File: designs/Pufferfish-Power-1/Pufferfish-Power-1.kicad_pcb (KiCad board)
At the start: 2 copper layers, 196 parts, among them J1 POWER_JACK_PTH, J2 POWER_JACK_PTH, J3 Molex_PicoFlex_20_Vertical, J4 Molex_MicroFit3_2x4_Receptacle, J5 Molex_MicroFit_2P, J6 Molex_MicroFit_2P, Q1 SiR158DP, Q10 2N7002E, Q11 2N7002E, Q12 2N7002E, Q13 2N7002E, Q14 2N7002E, Q14 TP0610T, Q15 2N7002E, Q15 TP0610T, Q16 2N7002E, Q16 TP0610T, Q17 2N7002E, Q17 TP0610T, Q18 2N7002E, Q18 TP0610T, Q19 2N7002E, Q19 TP0610T, Q2 SiR158DP, Q3 SiR158DP, Q4 SiR158DP, Q5 2N7002E, Q6 SiSS27DN, Q7 SiSS27DN, Q8 TP0610T, Q9 2N7002E, U1 LTC4421IUHE, U2 TPS568215RNN, U3 TPS82130

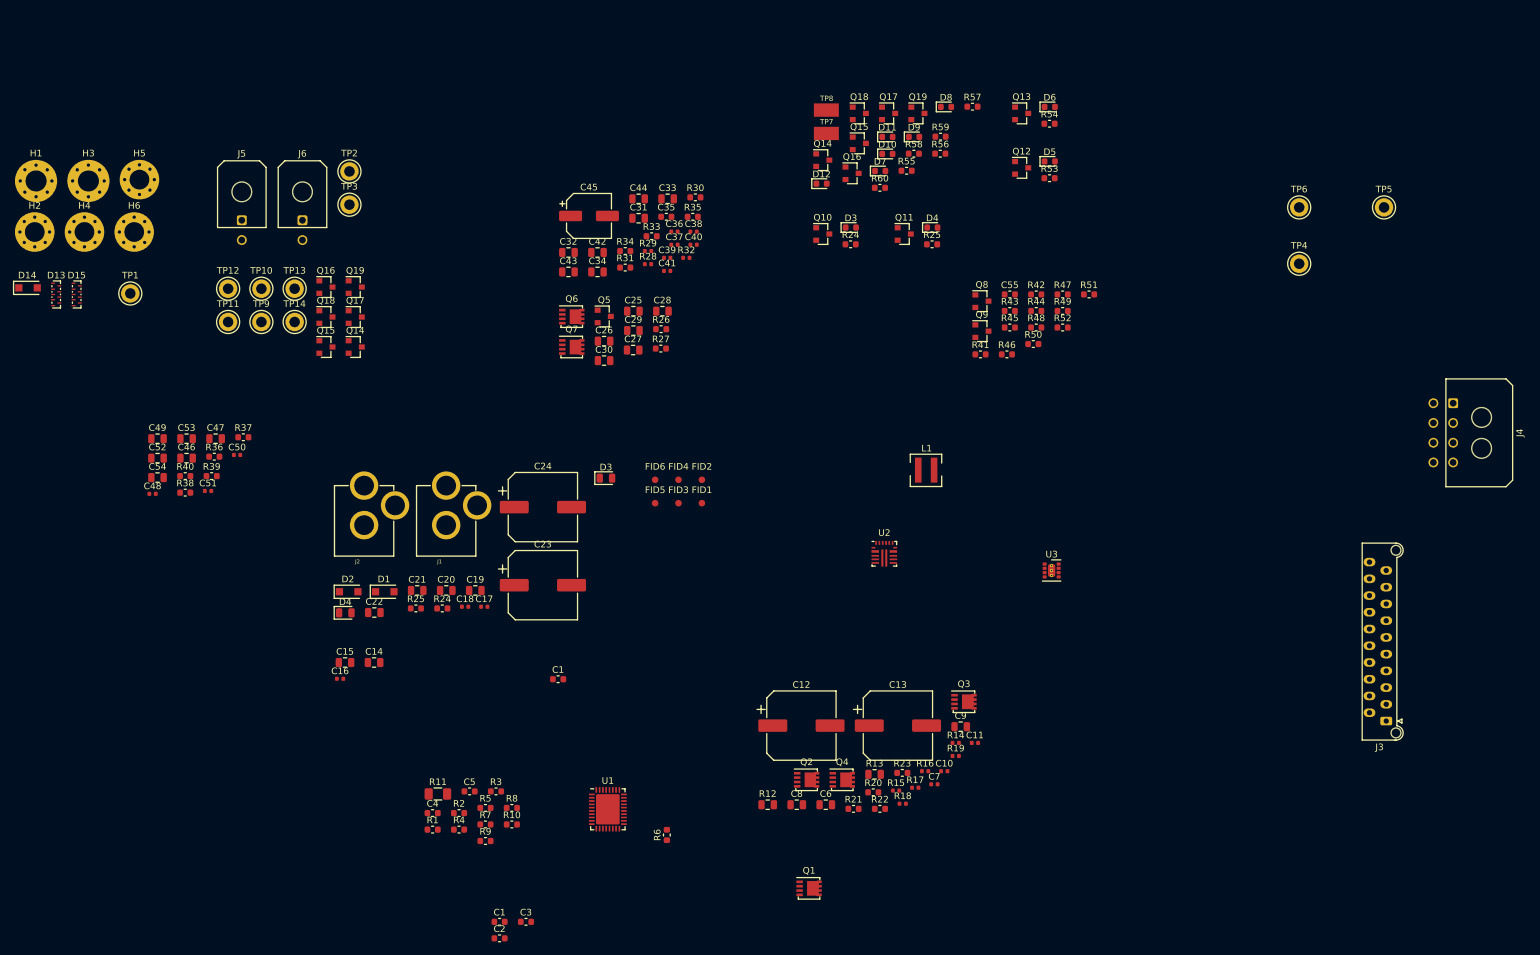
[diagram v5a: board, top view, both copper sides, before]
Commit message: Initial board layout, routing completed
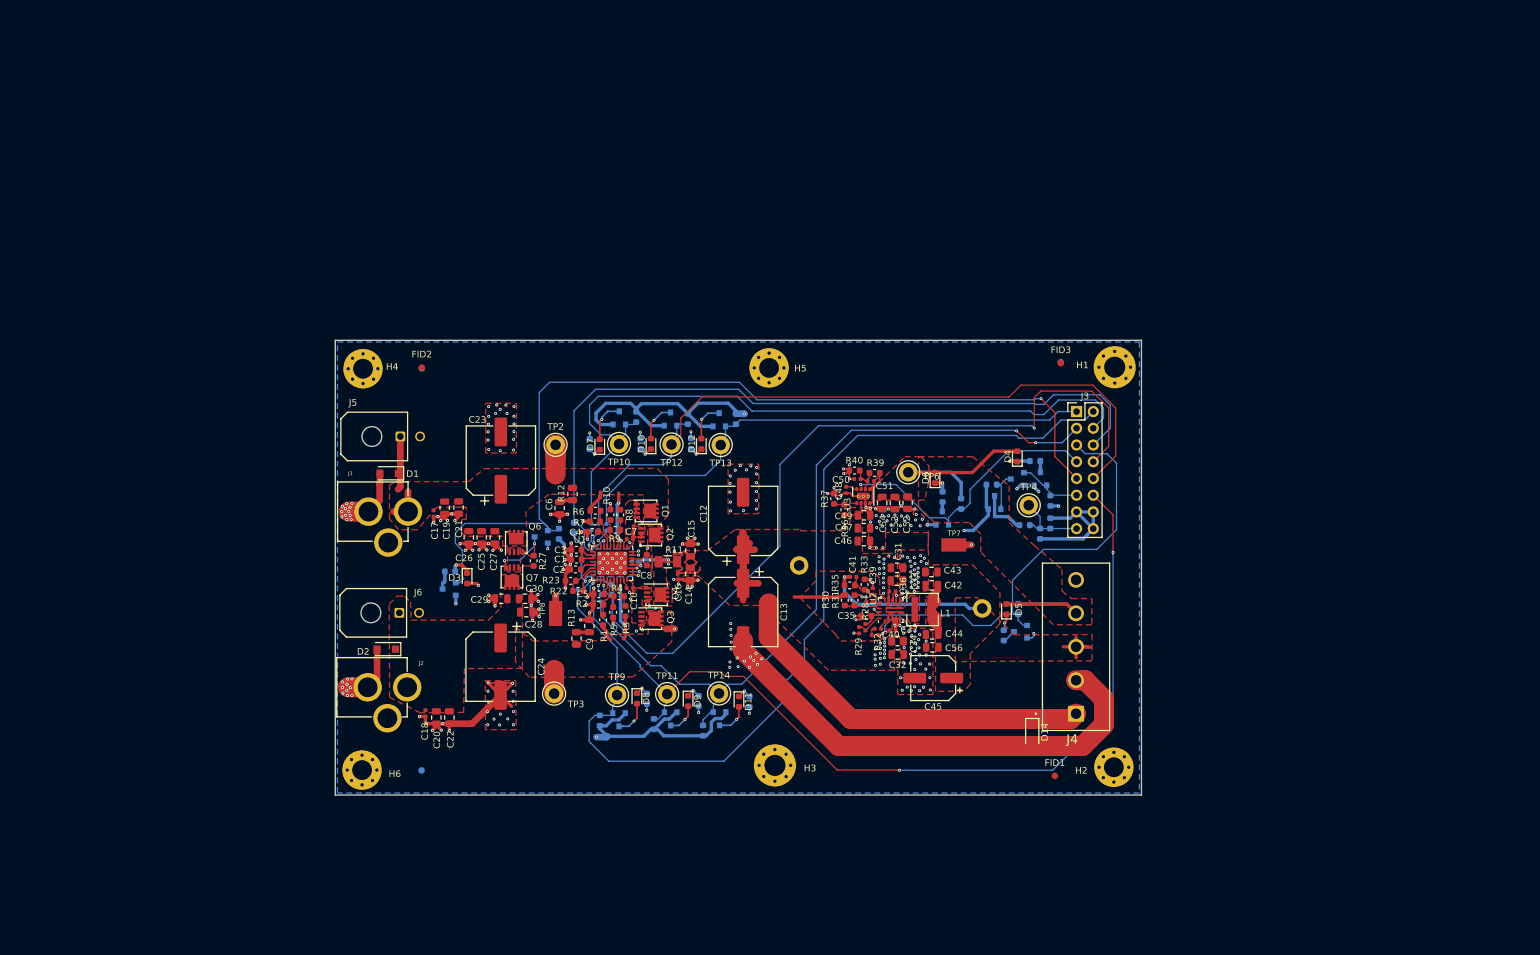
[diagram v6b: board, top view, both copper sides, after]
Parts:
- removed the C1 at (124.5, 119.4)
- removed D13, D15: ESDLC5V0PB8, Package_DFN_QFN:UDFN-9_1.0x3.8mm_P0.5mm
- removed the D3 at (168.9, 50.8)
- removed the D3 at (131.7, 88.8)
- removed the D4 at (92.2, 109.3)
- removed the Q14 at (164.6, 40.6)
- removed the Q15 at (170.2, 38.0)
- removed the Q16 at (169.1, 42.6)
- removed the Q17 at (174.6, 33.5)
- removed the Q18 at (170.2, 33.5)
- removed the Q19 at (179.1, 33.5)
- removed the R24 at (106.9, 108.6)
- removed the R25 at (102.9, 108.6)
- removed R45, R46: RES_10K_0603_SMD, Pufferfish:RES_SMD_0603
- added C56: CAP_22uF_25V_X5R_0805, Pufferfish:CAP_SMD_0805, F.Cu at (181.3, 114.5)
- added D3: LED_SMD_0603_YELLOW, LED_SMD:LED_0603_1608Metric, F.Cu at (110.6, 104.1)
- C11, C55, FID4, FID5, FID6, Q10, Q11, Q12, Q13, Q14, Q15, Q16, Q17, Q18, Q19, Q5, Q8, Q9, R14, R15, R16, R17, R18, R19, R20, R21, R24, R25, R26, R34, R38, R41, R42, R43, R44, R47, R48, R49, R50, R51, R52, R53, R54, R55, R56, R57, R58, R59, R60, TP1, TP5: moved to B.Cu
- C8: footprint Pufferfish:CAP_SMD_0805 -> Pufferfish:CAP_SMD_0603
- J3: value Molex_PicoFlex_20_Vertical -> 5103308-3; footprint Connector_Molex:Molex_Picoflex_90325-0020_2x10_P1.27mm_Vertical -> Connector_PinHeader_2.54mm:PinHeader_2x08_P2.54mm_Vertical
- J4: value Molex_MicroFit3_2x4_Receptacle -> Screw_Terminal_01x05; footprint Connector_Molex:Molex_Micro-Fit_3.0_43045-0800_2x04_P3.00mm_Horizontal -> Pufferfish:CUI_TB004-508-05BE
- moved H2 182.9 mm to (208.8, 132.7)
- moved D14 166.8 mm to (196.4, 127.5), turned to 270 degrees
- moved H1 166.2 mm to (209.0, 72.0)
- moved H3 136.9 mm to (157.4, 132.5)
- moved R38 117.8 mm to (185.6, 92.7), turned to 270 degrees
- moved C52 114.1 mm to (177.5, 92.6), turned to 270 degrees
- moved C54 110.1 mm to (173.7, 92.6), turned to 270 degrees
- moved TP1 109.6 mm to (161.1, 102.1)
- moved C53 108.0 mm to (175.6, 92.6), turned to 270 degrees
- moved C49 107.9 mm to (170.9, 94.5)
- moved C48 105.3 mm to (168.2, 90.7), turned to 270 degrees
- moved C46 103.6 mm to (170.9, 98.4)
- moved R40 101.6 mm to (169.5, 87.7), turned to 180 degrees
- moved D8 101.3 mm to (136.4, 122.3), turned to 270 degrees
- moved R39 100.7 mm to (172.5, 88.1), turned to 180 degrees
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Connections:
- net Net-(R22-Pad2) renamed /LTC4221/LTC4421-RETRY
- net Net-(R36-Pad2) renamed /3.3V Buck/3V3-EN
- C10 pad 1: /LTC4221/LTC4421-SOURCE2 -> /LTC4221/LTC4421-GATE2
- C10 pad 2: /LTC4221/LTC4421-GATE2 -> /LTC4221/LTC4421-SRC2
- C8 pad 2: VSYS-12V0 -> /LTC4221/LTC4421-CPO
- J3 pad 1: LTC4421-PWR-nDISABLE1 -> LTC4421-PWR-nCH1
- J3 pad 10: LTC4421-PWR-nCH2 -> LTC4421-PWR-nVALID1
- J3 pad 11: GND -> /Interface/BAT-MEAS-EN
- J3 pad 13: 3V3-PGOOD -> GND
- J3 pad 14: LTC4421-PWR-nFAULT2 -> GND
- J3 pad 15: GND -> /Interface/BAT-MEAS-ANALOG
- J3 pad 2: LTC4421-PWR-nCH1 -> LTC4421-PWR-nFAULT2
- J3 pad 3: GND -> LTC4421-PWR-nCH2
- J3 pad 4: LTC4421-PWR-nVALID1 -> LTC4421-PWR-nFAULT1
- J3 pad 5: LTC4421-PWR-nDISABLE2 -> VSYS-5V0-PGOOD
- J3 pad 6: LTC4421-PWR-nFAULT1 -> LTC4421-PWR-nDISABLE1
- J3 pad 7: GND -> 3V3-PGOOD
- J3 pad 8: BAT-CHARGE-EN -> LTC4421-PWR-nDISABLE2
- J3 pad 9: VSYS-5V0-PGOOD -> BAT-CHARGE-EN
- J4 pad 2: VSYS-12V0 -> GND
- J4 pad 3: GND -> VSYS-5V0
- J4 pad 4: GND -> VSYS-3V3
- J4 pad 5: VSYS-3V3 -> GND
- J6 pad 1: Net-(J6-Pad1) -> VIN-BACKUP-12V0
- Q3 pad 1: /LTC4221/LTC4421-GATE2 -> /LTC4221/LTC4421-SRC2
- Q3 pad 2: /LTC4221/LTC4421-GATE2 -> /LTC4221/LTC4421-SRC2
- Q3 pad 3: /LTC4221/LTC4421-GATE2 -> /LTC4221/LTC4421-SRC2
- Q3 pad 4: /LTC4221/LTC4421-SOURCE2 -> /LTC4221/LTC4421-GATE2
- Q4 pad 1: /LTC4221/LTC4421-GATE2 -> /LTC4221/LTC4421-SRC2
- Q4 pad 2: /LTC4221/LTC4421-GATE2 -> /LTC4221/LTC4421-SRC2
- Q4 pad 3: /LTC4221/LTC4421-GATE2 -> /LTC4221/LTC4421-SRC2
- Q4 pad 4: /LTC4221/LTC4421-SOURCE2 -> /LTC4221/LTC4421-GATE2
- TP3 pad 1: Net-(TP3-Pad1) -> VIN-BACKUP-12V0
- TP4 pad 1: Net-(Q8-Pad3) -> /Interface/BAT-MEAS-ANALOG
- TP5 pad 1: Net-(TP5-Pad1) -> VSYS-5V0
- U1 pad 27: /LTC4221/LTC4421-SOURCE2 -> /LTC4221/LTC4421-GATE2
- U1 pad 28: /LTC4221/LTC4421-GATE2 -> /LTC4221/LTC4421-SRC2
- U1 pad 33: VSYS-12V0 -> /LTC4221/LTC4421-CPO
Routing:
- net GND: track 0.00 -> 305.8 mm, vias 0 -> 293
- net VSYS-3V3: track 0.00 -> 254.7 mm, vias 0 -> 3
- net VSYS-12V0: track 0.00 -> 149.1 mm, vias 0 -> 35
- net LTC4421-PWR-nFAULT2: track 0.00 -> 145.8 mm
- net BAT-CHARGE-EN: track 0.00 -> 140.0 mm, vias 0 -> 1
- net LTC4421-PWR-nVALID2: track 0.00 -> 136.6 mm, vias 0 -> 2
- net LTC4421-PWR-nDISABLE2: track 0.00 -> 121.3 mm, vias 0 -> 2
- net LTC4421-PWR-nDISABLE1: track 0.00 -> 118.4 mm, vias 0 -> 1
- net LTC4421-PWR-nCH2: track 0.00 -> 116.4 mm, vias 0 -> 2
- net LTC4421-PWR-nFAULT1: track 0.00 -> 112.4 mm
- net LTC4421-PWR-nVALID1: track 0.00 -> 110.8 mm
- net LTC4421-PWR-nCH1: track 0.00 -> 83.4 mm
- net VIN-BACKUP-12V0: track 0.00 -> 78.3 mm, vias 0 -> 4
- net VSYS-5V0-PGOOD: track 0.00 -> 68.8 mm, vias 0 -> 1
- net VSYS-5V0: track 0.00 -> 46.9 mm, vias 0 -> 1
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- added copper zone on F.Cu, net /5V Buck/5V-BUCK-SW
- added copper zone on F.Cu, net /Input Connectors/CHARGER-DIODE
- added copper zone on F.Cu, net /LTC4221/LTC4421-SENSE
- added copper zone on F.Cu, net /LTC4221/LTC4421-SRC1
- added copper zone on F.Cu, net /LTC4221/LTC4421-SRC2
- added copper zone on B.Cu, net GND
- added copper zone on F.Cu, net GND
- added copper zone on In1.Cu, net GND
- added copper zone on In2.Cu, net GND
- added copper zone on F.Cu, net VIN-BACKUP-12V0
- added copper zone on F.Cu, net VIN-PRIMARY-12V0
- added copper zone on F.Cu, net VSYS-12V0
- added copper zone on In2.Cu, net VSYS-12V0
- added copper zone on F.Cu, net VSYS-3V3
- added copper zone on F.Cu, net VSYS-5V0
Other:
- board outline added: 122.4 x 69 mm
- copper layers 2 -> 4
- net class Default: clearance 0.2 -> 0.1524; trace_width 0.25 -> 0.1016; via_dia 0.8 -> 0.4572; via_drill 0.4 -> 0.2032
- rule pad_to_mask_clearance: 0.051 -> 0.0508
- rule solder_mask_min_width: 0.25 -> 0.254
- rule trace_clearance: 0.2 -> 0.1524
- rule trace_min: 0.2 -> 0.0762
- rule via_min_drill: 0.3 -> 0.1524
- rule via_min_size: 0.4 -> 0.3556

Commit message: - Added gerbers - Updated layout with silkscreen and DRC
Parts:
- added G***: LOGO, Pufferfish:LOGO_PUFFERFISH, F.Cu at (161.6, 84.2)
- TP1: moved to F.Cu
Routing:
- net GND: track 305.8 -> 301.4 mm, vias 293 -> 830
- net VIN-PRIMARY-12V0: track 33.2 -> 31.0 mm
- net VSYS-5V0: track 46.9 -> 45.5 mm
- net VSYS-12V0: track 149.1 -> 147.9 mm, vias 35 -> 34
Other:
- board text added: "1"
- board text added: "12V"
- board text added: "12V Backup"
- board text added: "12V Out"
- board text added: "12V Primary"
- board text added: "15"
- board text added: "16"
- board text added: "2"
- board text added: "3.3V"
- board text added: "3.3V PGOOD"
- board text added: "5V"
- board text added: "5V PGOOD"
- board text added: "Batt. Meas. Active"
- board text added: "Batt. Measurement"
- board text added: "Control Interface"
- board text added: "GND"
- board text added: "Power Module v1.0"
- board text added: "Power Output"
- board text added: "Primary Active"
- board text added: "Primary Fault"
- board text added: "Primary Valid"
- board text added: "Pufferfish"
- board text added: "S/N"
- board text added: "Secondary Active"
- board text added: "Secondary Fault"
- board text added: "Secondary Valid"

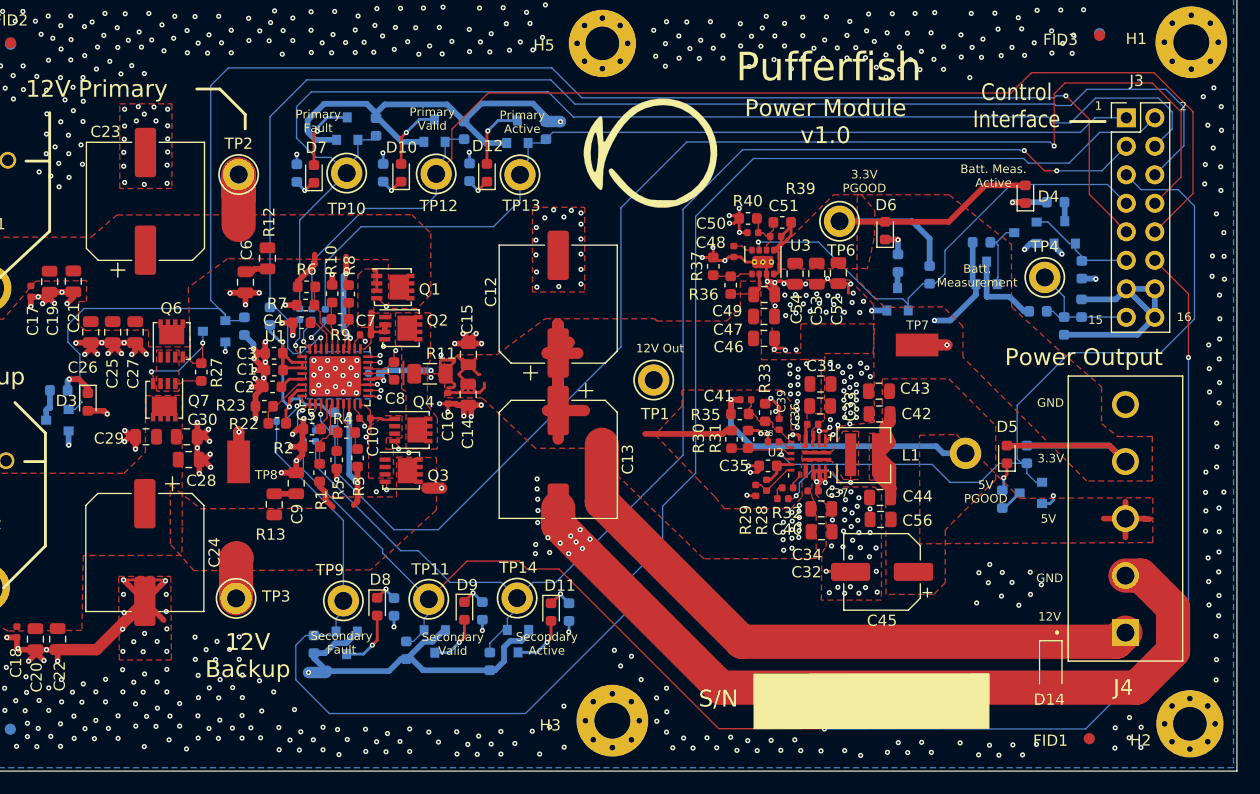
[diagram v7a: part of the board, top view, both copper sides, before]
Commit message: - Updated track width per DFM recommendations
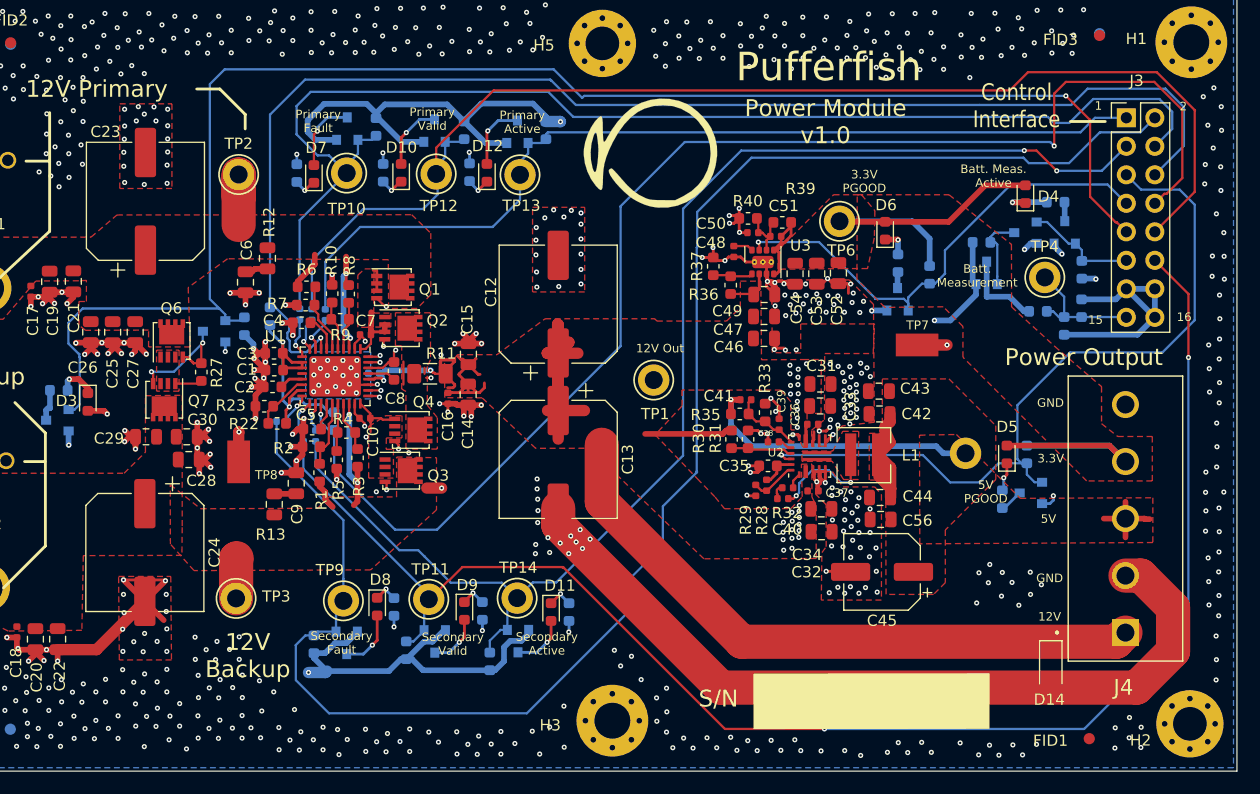
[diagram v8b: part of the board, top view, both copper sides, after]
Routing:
- net BAT-CHARGE-EN: track 140.0 -> 138.7 mm
- net /LTC4221/LTC4421-SENSE: track 18.2 -> 17.0 mm
- net VSYS-12V0: track 147.9 -> 146.9 mm
- net 3V3-PGOOD: track 43.0 -> 43.7 mm
- net VSYS-5V0-PGOOD: track 68.8 -> 69.5 mm
- net LTC4421-PWR-nDISABLE2: track 121.3 -> 121.9 mm
- net /LTC4221/LTC4421-SRC2: track 5.72 -> 5.12 mm
- net /Input Connectors/CHARGER-GATE: track 11.7 -> 12.3 mm
- net LTC4421-PWR-nVALID2: track 136.6 -> 136.1 mm
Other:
- net class Default: trace_width 0.1016 -> 0.2032
- rule trace_min: 0.0762 -> 0.1524
